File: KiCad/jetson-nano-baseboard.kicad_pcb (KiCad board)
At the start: 8 copper layers, 100.2 x 55 mm, 325 parts, among them IC1 TCA9548ARGER, IC10 TPS62823DLCT, IC11 SN74LV1T125DCKR, IC12 74HC00PW, IC13 SN74LVC1G126DCKR, IC15 TLV70018DCKT, IC16 NCP380HSNAJAAT1G, IC17 AT24CS01-ST, IC3 TPS54561, IC4 TLV70018DCKT, IC6 PCA9517ADP, IC7 HD3SS3220, IC8 LM3671MF-3.3, IC9 LM3671MF-3.3, J1 685119136923, J11 632723300011, J2 2129320-3, J6 WE_68715014522, J7 WE_68715014022, Q1 PMV32UP, T1 BSS138APW, T2 BSS138APW, T3 BSS138APW, T4 BSS138APW, T5 BSS138APW, T6 BSS138APW

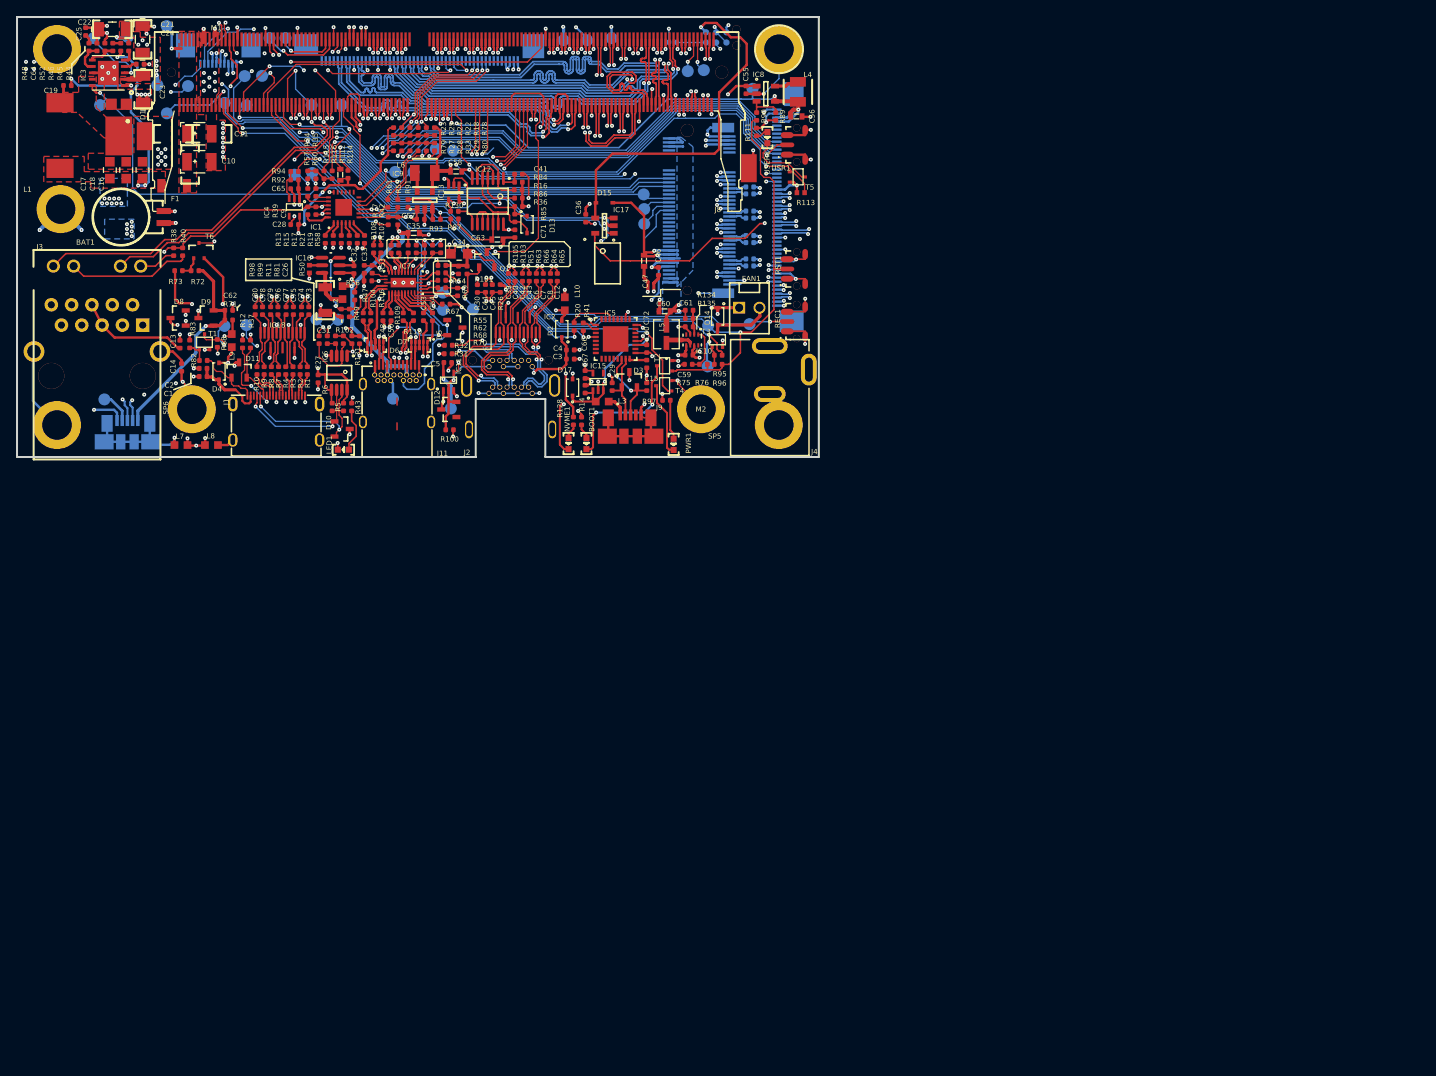
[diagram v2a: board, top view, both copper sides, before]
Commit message: Add PCB stackup table
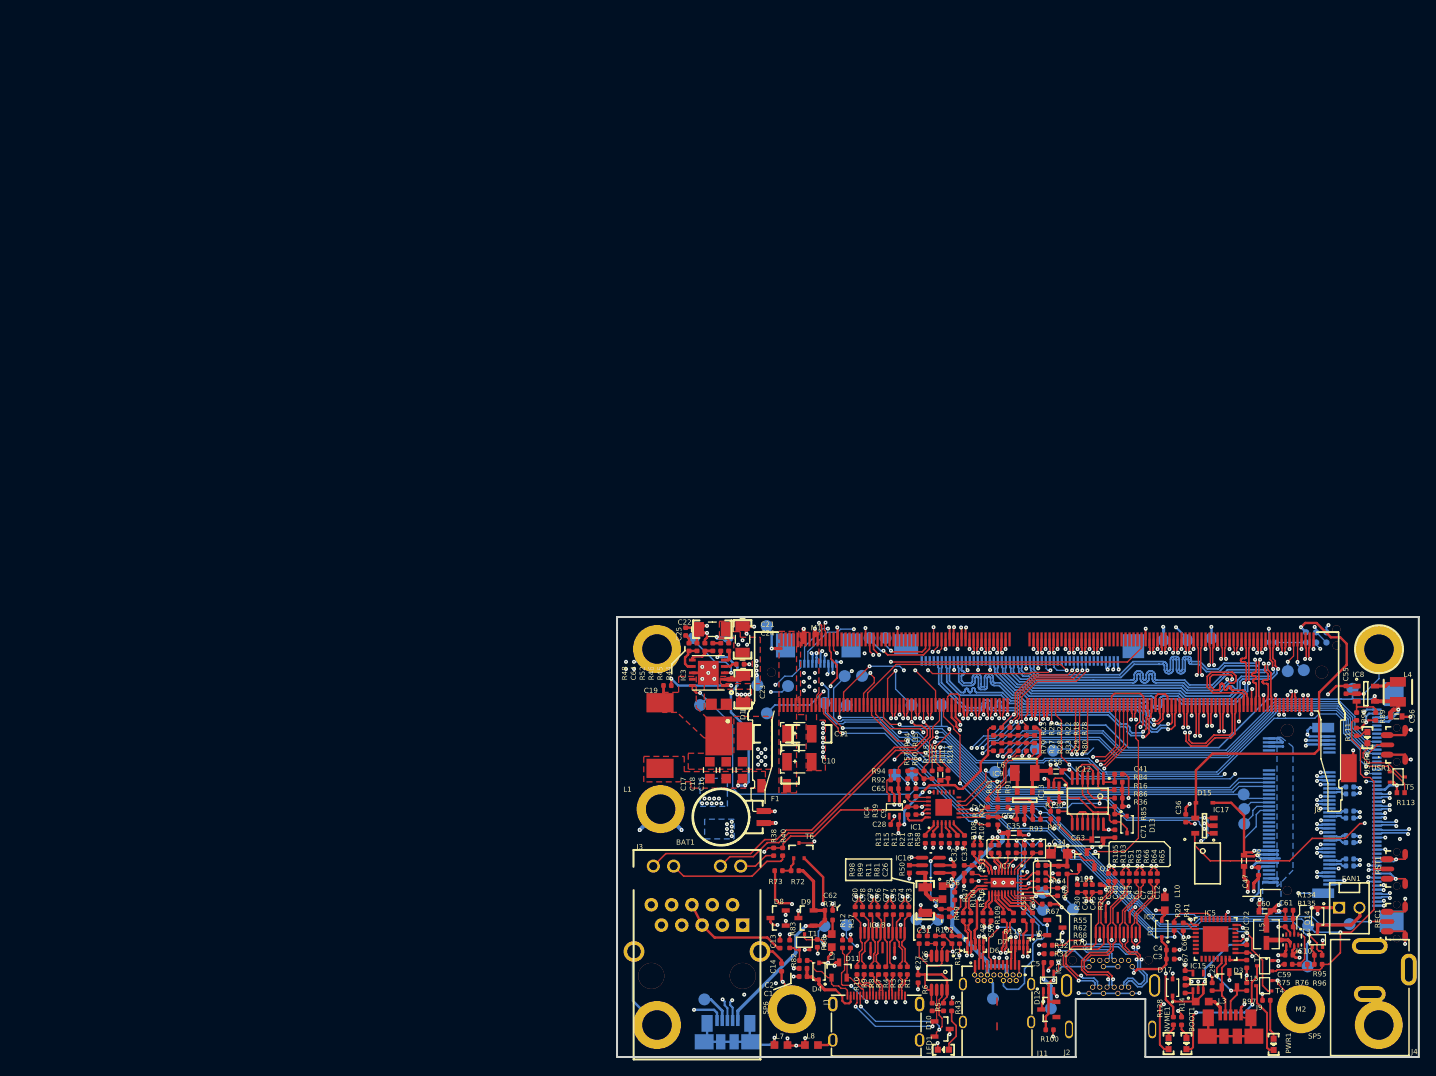
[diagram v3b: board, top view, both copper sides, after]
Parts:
- moved BAT1 106.1 mm to (93.3, 99.9)
- moved BOOT1 106.1 mm to (146.1, 128.2)
- moved C1 106.1 mm to (98.2, 119.8)
- moved C10 106.1 mm to (96.2, 93.0)
- moved C11 106.1 mm to (96.2, 89.5)
- moved C12 106.1 mm to (142.5, 107.4)
- moved C13 106.1 mm to (95.3, 115.8)
- moved C14 106.1 mm to (95.5, 118.7)
- moved C15 106.1 mm to (153.7, 121.1)
- moved C16 106.1 mm to (90.6, 94.1)
- moved C17 106.1 mm to (86.6, 94.1)
- moved C18 106.1 mm to (88.6, 94.1)
- moved C19 106.1 mm to (81.3, 83.5)
- moved C2 106.1 mm to (98.2, 118.8)
- moved C21 106.1 mm to (90.7, 77.7)
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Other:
- board text added: "0.018 mm"
- board text added: "0.02 mm"
- board text added: "0.035 mm"
- board text added: "0.12 mm"
- board text added: "0.2 mm"
- board text added: "0.24 mm"
- board text added: "1"
- board text added: "10"
- board text added: "11"
- board text added: "12"
- board text added: "13"
- board text added: "14"
- board text added: "15"
- board text added: "16"
- board text added: "17"
- board text added: "2"
- board text added: "3"
- board text added: "3.5"
- board text added: "4"
- board text added: "4.2"
- board text added: "5"
- board text added: "6"
- board text added: "7"
- board text added: "8"
- board text added: "9"
- board text added: "Bottom Layer"
- board text added: "Bottom Solder"
- board text added: "Constant"
- board text added: "Copper"
- board text added: "Dielectric 1"
- board text added: "Dielectric 2"
- board text added: "Dielectric 3"
- board text added: "Dielectric 4"
- board text added: "Dielectric 5"
- board text added: "Dielectric 6"
- board text added: "Dielectric 7"
- board text added: "FR-4"
- board text added: "Gold plating (ENIG, selective)"
- board text added: "Layer"
- board text added: "Material"
- board text added: "Name"
- board text added: "Prepreg"
- board text added: "Recommended PCB finish:"
- board text added: "Recommended PCB stackup"
- board text added: "Signal 1"
- board text added: "Signal 2"
- board text added: "Signal 3"
- board text added: "Signal 4"
- board text added: "Signal 5"
- board text added: "Signal 6"
- board text added: "Silkscreen: white"
- board text added: "Solder Resist"
- board text added: "Solder mask: matt black"
- board text added: "Suggested prepreg material is ISOLA PR2116"
- board text added: "The design includes high speed signaling"
- board text added: "Thickness"
- board text added: "Top Layer"
- board text added: "Top Solder"
- board text removed: "BAT1"
- board text removed: "BOOT"
- board text removed: "C1"
- board text removed: "C14"
- board text removed: "C15"
- board text removed: "C16"
- board text removed: "C17"
- board text removed: "C18"
- board text removed: "C19"
- board text removed: "C2"
- board text removed: "C21"
- board text removed: "C23"
- board text removed: "C24"
- board text removed: "C3"
- board text removed: "C31"
- board text removed: "C36"
- board text removed: "C37"
- board text removed: "C38"
- board text removed: "C4"
- board text removed: "C41"
- board text removed: "C49"
- board text removed: "C5"
- board text removed: "C51"
- board text removed: "C52"
- board text removed: "C59"
- board text removed: "C60"
- board text removed: "C61"
- board text removed: "C62"
- board text removed: "C63"
- board text removed: "C64"
- board text removed: "C68"
- board text removed: "C69"
- board text removed: "C70"
- board text removed: "C71"
- board text removed: "C9"
- board text removed: "D10"
- board text removed: "D11"
- board text removed: "D13"
- board text removed: "D17"
- board text removed: "D3"
- board text removed: "D4"
- board text removed: "D6"
- board text removed: "D7"
- board text removed: "D8"
- board text removed: "D9"
- board text removed: "FAN"
- board text removed: "IC1"
- board text removed: "IC12"
- board text removed: "IC16"
- board text removed: "IC18"
- board text removed: "IC2"
- board text removed: "IC3"
- board text removed: "IC4"
- board text removed: "IC6"
- board text removed: "IC7"
- board text removed: "IC9"
- board text removed: "J1"
- board text removed: "J10"
- board text removed: "J11"
- board text removed: "J2"
- board text removed: "J3"
- board text removed: "J4"
- board text removed: "J5"
- board text removed: "J7"
- board text removed: "J8"
- board text removed: "L1"
- board text removed: "L10"
- board text removed: "L3"
- board text removed: "L4"
- board text removed: "L5"
- board text removed: "L6"
- board text removed: "L7"
- board text removed: "L8"
- board text removed: "LED1"
- board text removed: "M1"
- board text removed: "PWR"
- board text removed: "Q1"
- board text removed: "R101"
- board text removed: "R102"
- board text removed: "R104"
- board text removed: "R106"
- board text removed: "R110"
- board text removed: "R112"
- board text removed: "R113"
- board text removed: "R114"
- board text removed: "R115"
- board text removed: "R116"
- board text removed: "R12"
- board text removed: "R128"
- board text removed: "R132"
- board text removed: "R134"
- board text removed: "R135"
- board text removed: "R14"
- board text removed: "R16"
- board text removed: "R20"
- board text removed: "R34"
- board text removed: "R35"
- board text removed: "R36"
- board text removed: "R37"
- board text removed: "R39"
- board text removed: "R41"
- board text removed: "R44"
- board text removed: "R45"
- board text removed: "R46"
- board text removed: "R47"
- board text removed: "R48"
- board text removed: "R49"
- board text removed: "R52"
- board text removed: "R53"
- board text removed: "R56"
- board text removed: "R57"
- board text removed: "R59"
- board text removed: "R60"
- board text removed: "R61"
- board text removed: "R71"
- board text removed: "R72"
- board text removed: "R73"
- board text removed: "R75"
- board text removed: "R76"
- board text removed: "R84"
- board text removed: "R85"
- board text removed: "R86"
- board text removed: "R91"
- board text removed: "R93"
- board text removed: "R97"
- board text removed: "REC"
- board text removed: "RST"
- board text removed: "SP1"
- board text removed: "SP2"
- board text removed: "SP3"
- board text removed: "SP4"
- board text removed: "SP6"
- board text removed: "SP7"
- board text removed: "T2"
- board text removed: "T4"
- board text removed: "T5"
- board text removed: "TP1"
- board text removed: "TP10"
- board text removed: "TP11"
- board text removed: "TP12"
- board text removed: "TP13"
- board text removed: "TP14"
- board text removed: "TP15"
- board text removed: "TP16"
- board text removed: "TP17"
- board text removed: "TP18"
- board text removed: "TP19"
- board text removed: "TP2"
- board text removed: "TP20"
- board text removed: "TP21"
- board text removed: "TP22"
- board text removed: "TP23"
- board text removed: "TP24"
- board text removed: "TP25"
- board text removed: "TP26"
- board text removed: "TP27"
- board text removed: "TP28"
- board text removed: "TP29"
- board text removed: "TP3"
- board text removed: "TP30"
- board text removed: "TP31"
- board text removed: "TP32"
- board text removed: "TP33"
- board text removed: "TP34"
- board text removed: "TP35"
- board text removed: "TP36"
- board text removed: "TP37"
- board text removed: "TP38"
- board text removed: "TP39"
- board text removed: "TP4"
- board text removed: "TP40"
- board text removed: "TP41"
- board text removed: "TP42"
- board text removed: "TP43"
- board text removed: "TP44"
- board text removed: "TP45"
- board text removed: "TP47"
- board text removed: "TP5"
- board text removed: "TP6"
- board text removed: "TP7"
- board text removed: "TP8"
- board text removed: "TP9"
